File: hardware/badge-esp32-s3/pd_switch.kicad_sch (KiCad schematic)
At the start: 2 parts

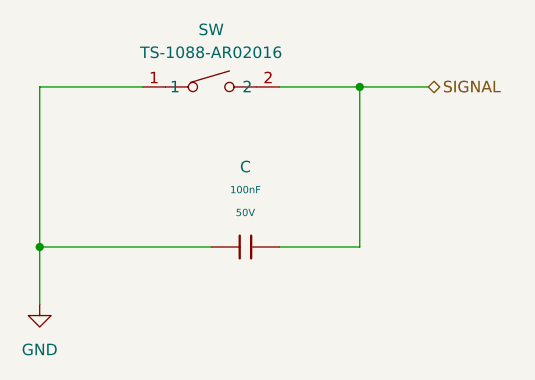
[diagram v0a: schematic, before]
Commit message: add display block
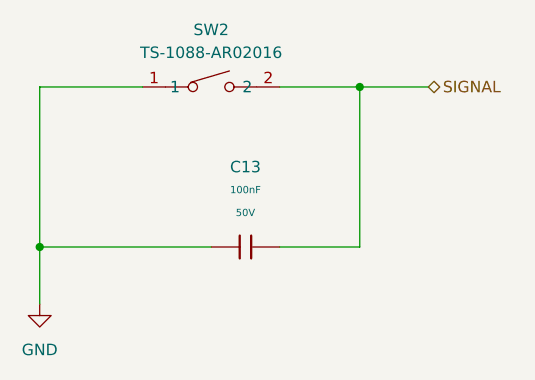
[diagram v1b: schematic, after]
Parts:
- renumbered C to C13, SW to SW2
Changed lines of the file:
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@@
 		(dnp no)
 		(fields_autoplaced yes)
-		(property "Reference" "C"
+		(property "Reference" "C13"
 			(at 143.51 95.25 90)
 			(effects
@@
 				(path "/e2af9a6c-dbe9-4de2-9ba6-ea213a7300ec/ac5926f6-d694-4e07-a059-1576f5340396"
 					(reference "C12")
+					(unit 1)
+				)
+				(path "/e2af9a6c-dbe9-4de2-9ba6-ea213a7300ec/b79c388b-f340-4022-8bff-2018e70f780a"
+					(reference "C13")
 					(unit 1)
 				)
@@
 		(dnp no)
 		(fields_autoplaced yes)
-		(property "Reference" "SW"
+		(property "Reference" "SW?"
 			(at 139.7 80.01 0)
 			(effects
@@
 				(path "/e2af9a6c-dbe9-4de2-9ba6-ea213a7300ec/ac5926f6-d694-4e07-a059-1576f5340396"
 					(reference "SW2")
+					(unit 1)
+				)
+				(path "/e2af9a6c-dbe9-4de2-9ba6-ea213a7300ec/b79c388b-f340-4022-8bff-2018e70f780a"
+					(reference "SW?")
 					(unit 1)
 				)
@@
 		(dnp no)
 		(fields_autoplaced yes)
-		(property "Reference" "#PWR"
+		(property "Reference" "#PWR0101"
 			(at 120.65 116.84 0)
 			(effects
@@
 					(unit 1)
 				)
+				(path "/e2af9a6c-dbe9-4de2-9ba6-ea213a7300ec/b79c388b-f340-4022-8bff-2018e70f780a"
+					(reference "#PWR0101")
+					(unit 1)
+				)
